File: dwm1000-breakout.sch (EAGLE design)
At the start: 9 parts, among them U2 DWM1000

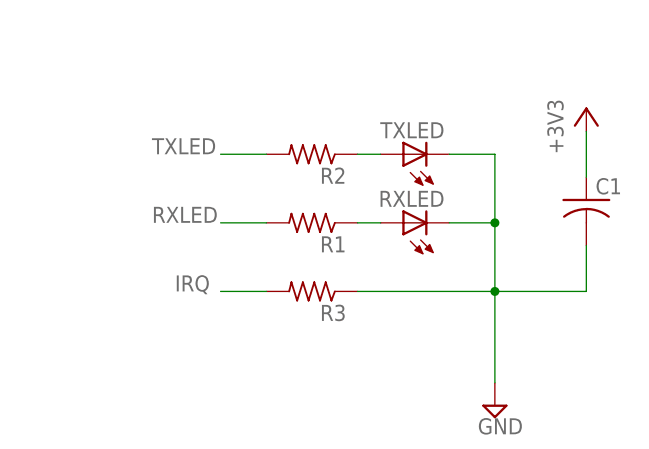
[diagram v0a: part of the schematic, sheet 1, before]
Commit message: renamed and laid out a little better i hope
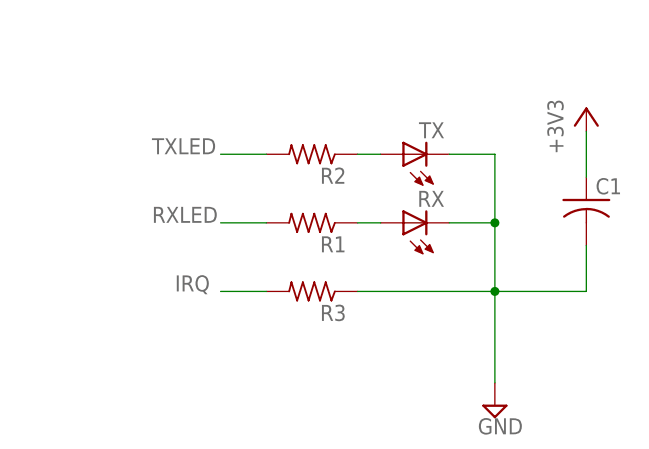
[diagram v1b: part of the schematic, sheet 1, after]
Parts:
- renumbered RXLED to RX, TXLED to TX
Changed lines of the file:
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@@
 <part name="R2" library="rcl" library_urn="urn:adsk.eagle:library:334" deviceset="R-US_" device="R1206"/>
 <part name="R3" library="rcl" library_urn="urn:adsk.eagle:library:334" deviceset="R-US_" device="R1206"/>
-<part name="RXLED" library="led" library_urn="urn:adsk.eagle:library:259" deviceset="LED" device="SMT1206"/>
-<part name="TXLED" library="led" library_urn="urn:adsk.eagle:library:259" deviceset="LED" device="SMT1206"/>
+<part name="RX" library="led" library_urn="urn:adsk.eagle:library:259" deviceset="LED" device="SMT1206"/>
+<part name="TX" library="led" library_urn="urn:adsk.eagle:library:259" deviceset="LED" device="SMT1206"/>
 <part name="SUPPLY1" library="supply2" library_urn="urn:adsk.eagle:library:372" deviceset="GND" device=""/>
 <part name="+3V1" library="supply1" library_urn="urn:adsk.eagle:library:371" deviceset="+3V3" device=""/>
@@
 <instance part="R2" gate="G$1" x="180.34" y="43.18" rot="R180"/>
 <instance part="R3" gate="G$1" x="180.34" y="27.94" rot="R180"/>
-<instance part="RXLED" gate="G$1" x="190.5" y="35.56" rot="R90"/>
-<instance part="TXLED" gate="G$1" x="190.5" y="43.18" rot="R90"/>
+<instance part="RX" gate="G$1" x="190.5" y="35.56" rot="R90"/>
+<instance part="TX" gate="G$1" x="190.5" y="43.18" rot="R90"/>
 <instance part="SUPPLY1" gate="GND" x="200.66" y="15.24"/>
 <instance part="+3V1" gate="G$1" x="210.82" y="48.26"/>
@@
 </segment>
 <segment>
-<pinref part="TXLED" gate="G$1" pin="C"/>
+<pinref part="TX" gate="G$1" pin="C"/>
 <wire x1="195.58" y1="43.18" x2="200.66" y2="43.18" width="0.1524" layer="91"/>
 <wire x1="200.66" y1="43.18" x2="200.66" y2="35.56" width="0.1524" layer="91"/>
 <pinref part="SUPPLY1" gate="GND" pin="GND"/>
-<pinref part="RXLED" gate="G$1" pin="C"/>
+<pinref part="RX" gate="G$1" pin="C"/>
 <wire x1="200.66" y1="35.56" x2="200.66" y2="27.94" width="0.1524" layer="91"/>
 <wire x1="200.66" y1="27.94" x2="200.66" y2="17.78" width="0.1524" layer="91"/>
@@
 <segment>
 <pinref part="R1" gate="G$1" pin="1"/>
-<pinref part="RXLED" gate="G$1" pin="A"/>
+<pinref part="RX" gate="G$1" pin="A"/>
 <wire x1="185.42" y1="35.56" x2="187.96" y2="35.56" width="0.1524" layer="91"/>
 </segment>
@@
 <segment>
 <pinref part="R2" gate="G$1" pin="1"/>
-<pinref part="TXLED" gate="G$1" pin="A"/>
+<pinref part="TX" gate="G$1" pin="A"/>
 <wire x1="185.42" y1="43.18" x2="187.96" y2="43.18" width="0.1524" layer="91"/>
 </segment>

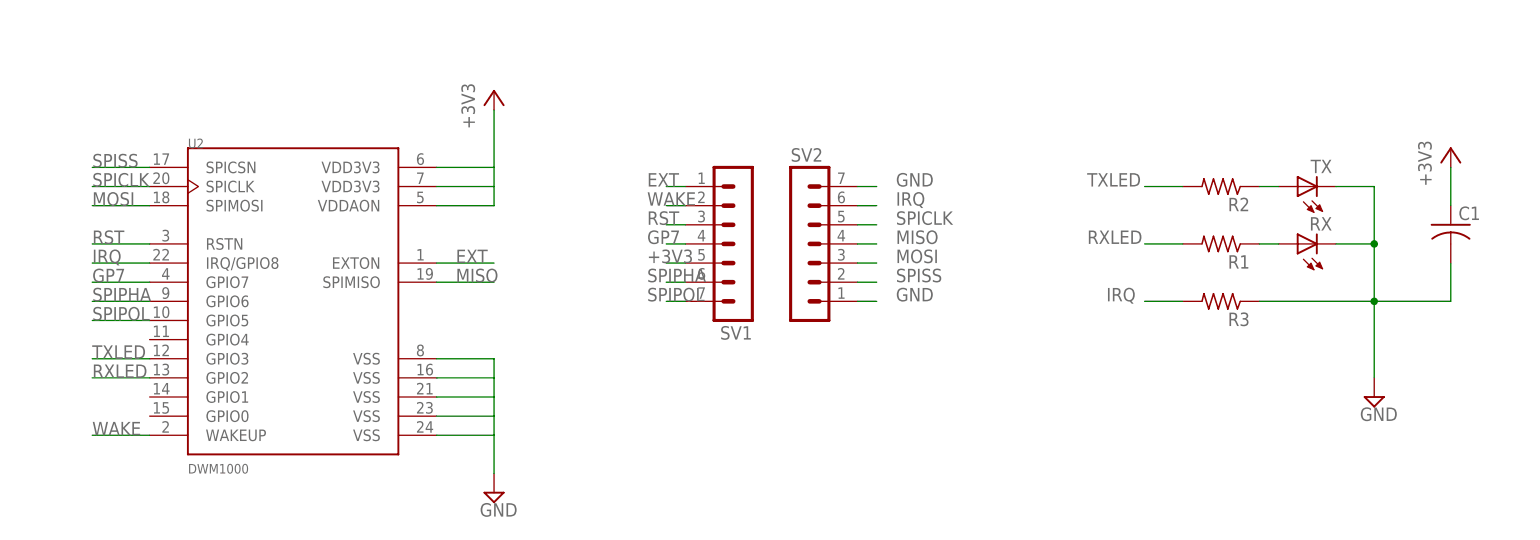
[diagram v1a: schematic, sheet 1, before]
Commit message: used oshpark's DRU file
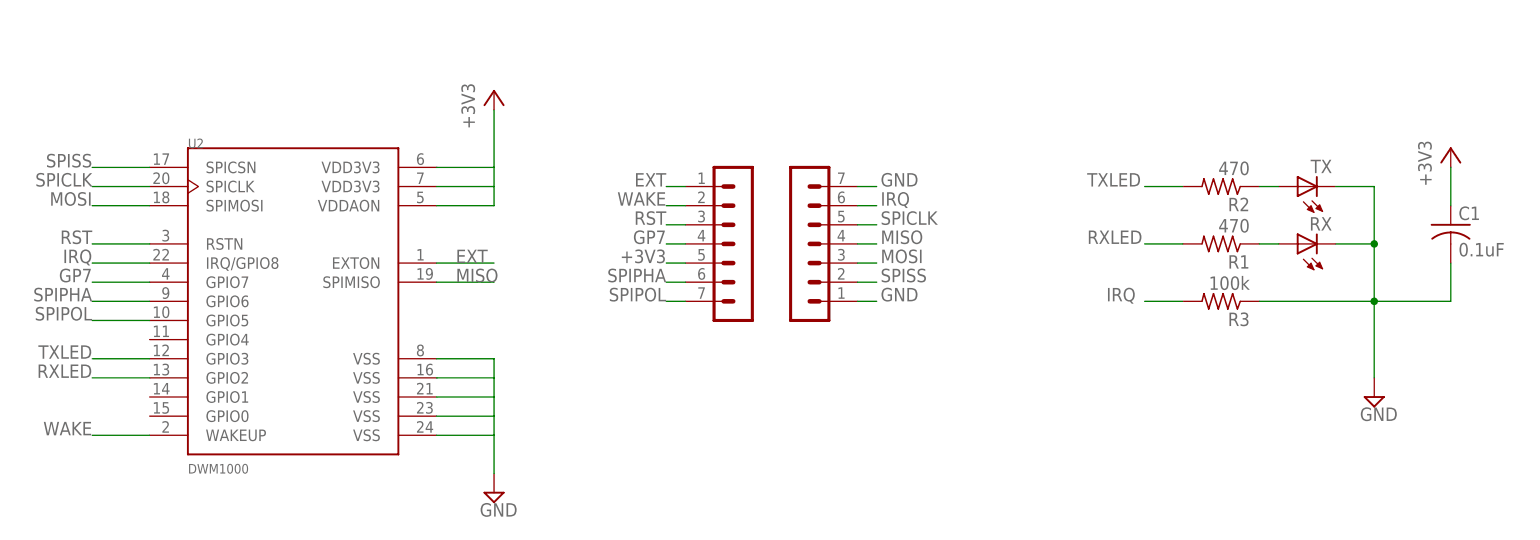
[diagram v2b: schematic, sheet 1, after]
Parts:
- C1: value (none) -> 0.1uF
- R1, R2: value (none) -> 470
- R3: value (none) -> 100k
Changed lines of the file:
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@@
 <setting verticaltext="up"/>
 </settings>
-<grid distance="0.1" unitdist="inch" unit="inch" style="dots" multiple="1" display="yes" altdistance="0.01" altunitdist="inch" altunit="inch"/>
+<grid distance="0.1" unitdist="inch" unit="inch" style="lines" multiple="1" display="no" altdistance="0.01" altunitdist="inch" altunit="inch"/>
 <layers>
 <layer number="1" name="Top" color="4" fill="1" visible="no" active="no"/>
@@
 <part name="SV1" library="con-lstb" library_urn="urn:adsk.eagle:library:162" deviceset="MA07-1" device=""/>
 <part name="SV2" library="con-lstb" library_urn="urn:adsk.eagle:library:162" deviceset="MA07-1" device=""/>
-<part name="C1" library="rcl" library_urn="urn:adsk.eagle:library:334" deviceset="C-US" device="C1206"/>
-<part name="R1" library="rcl" library_urn="urn:adsk.eagle:library:334" deviceset="R-US_" device="R1206"/>
-<part name="R2" library="rcl" library_urn="urn:adsk.eagle:library:334" deviceset="R-US_" device="R1206"/>
-<part name="R3" library="rcl" library_urn="urn:adsk.eagle:library:334" deviceset="R-US_" device="R1206"/>
+<part name="C1" library="rcl" library_urn="urn:adsk.eagle:library:334" deviceset="C-US" device="C1206" value="0.1uF"/>
+<part name="R1" library="rcl" library_urn="urn:adsk.eagle:library:334" deviceset="R-US_" device="R1206" value="470"/>
+<part name="R2" library="rcl" library_urn="urn:adsk.eagle:library:334" deviceset="R-US_" device="R1206" value="470"/>
+<part name="R3" library="rcl" library_urn="urn:adsk.eagle:library:334" deviceset="R-US_" device="R1206" value="100k"/>
 <part name="RX" library="led" library_urn="urn:adsk.eagle:library:259" deviceset="LED" device="SMT1206"/>
 <part name="TX" library="led" library_urn="urn:adsk.eagle:library:259" deviceset="LED" device="SMT1206"/>
@@
 </plain>
 <instances>
-<instance part="U2" gate="G$1" x="55.88" y="27.94"/>
+<instance part="U2" gate="G$1" x="55.88" y="27.94" smashed="yes">
+<attribute name="NAME" x="43.18" y="48.26" size="1.27" layer="95"/>
+<attribute name="VALUE" x="43.18" y="5.08" size="1.27" layer="96"/>
+</instance>
 <instance part="SUPPLY4" gate="GND" x="83.82" y="2.54"/>
 <instance part="+3V3" gate="G$1" x="83.82" y="55.88"/>
-<instance part="SV1" gate="1" x="116.84" y="35.56" rot="R180"/>
-<instance part="SV2" gate="1" x="124.46" y="35.56"/>
+<instance part="SV1" gate="1" x="116.84" y="35.56" smashed="yes" rot="R180">
+<attribute name="VALUE" x="118.11" y="48.26" size="1.778" layer="96" rot="R180"/>
+</instance>
+<instance part="SV2" gate="1" x="124.46" y="35.56" smashed="yes">
+<attribute name="VALUE" x="123.19" y="22.86" size="1.778" layer="96"/>
+</instance>
 <instance part="C1" gate="G$1" x="210.82" y="38.1"/>
 <instance part="R1" gate="G$1" x="180.34" y="35.56" rot="R180"/>
@@
 <pinref part="SV2" gate="1" pin="7"/>
 <wire x1="132.08" y1="43.18" x2="134.62" y2="43.18" width="0.1524" layer="91"/>
-<label x="137.16" y="43.18" size="1.778" layer="95"/>
+<label x="135.128" y="43.18" size="1.778" layer="95"/>
 </segment>
 <segment>
 <pinref part="SV2" gate="1" pin="1"/>
 <wire x1="132.08" y1="27.94" x2="134.62" y2="27.94" width="0.1524" layer="91"/>
-<label x="137.16" y="27.94" size="1.778" layer="95"/>
+<label x="135.128" y="27.94" size="1.778" layer="95"/>
 </segment>
 <segment>
@@
 <pinref part="SV1" gate="1" pin="5"/>
 <wire x1="109.22" y1="33.02" x2="106.68" y2="33.02" width="0.1524" layer="91"/>
-<label x="104.14" y="33.02" size="1.778" layer="95"/>
+<label x="106.68" y="33.02" size="1.778" layer="95" rot="MR0"/>
 </segment>
 <segment>
@@
 <pinref part="U2" gate="G$1" pin="SPIMOSI"/>
 <wire x1="38.1" y1="40.64" x2="30.48" y2="40.64" width="0.1524" layer="91"/>
-<label x="30.48" y="40.64" size="1.778" layer="95"/>
+<label x="30.48" y="40.64" size="1.778" layer="95" rot="MR0"/>
 </segment>
 <segment>
 <pinref part="SV2" gate="1" pin="3"/>
 <wire x1="132.08" y1="33.02" x2="134.62" y2="33.02" width="0.1524" layer="91"/>
-<label x="137.16" y="33.02" size="1.778" layer="95"/>
+<label x="135.128" y="33.02" size="1.778" layer="95"/>
 </segment>
 </net>
@@
 <pinref part="SV2" gate="1" pin="4"/>
 <wire x1="132.08" y1="35.56" x2="134.62" y2="35.56" width="0.1524" layer="91"/>
-<label x="137.16" y="35.56" size="1.778" layer="95"/>
+<label x="135.128" y="35.56" size="1.778" layer="95"/>
 </segment>
 </net>
@@
 <pinref part="U2" gate="G$1" pin="SPICLK"/>
 <wire x1="38.1" y1="43.18" x2="30.48" y2="43.18" width="0.1524" layer="91"/>
-<label x="30.48" y="43.18" size="1.778" layer="95"/>
+<label x="30.48" y="43.18" size="1.778" layer="95" rot="MR0"/>
 </segment>
 <segment>
 <pinref part="SV2" gate="1" pin="5"/>
 <wire x1="132.08" y1="38.1" x2="134.62" y2="38.1" width="0.1524" layer="91"/>
-<label x="137.16" y="38.1" size="1.778" layer="95"/>
+<label x="135.128" y="38.1" size="1.778" layer="95"/>
 </segment>
 </net>
@@
 <pinref part="U2" gate="G$1" pin="SPICSN"/>
 <wire x1="38.1" y1="45.72" x2="30.48" y2="45.72" width="0.1524" layer="91"/>
-<label x="30.48" y="45.72" size="1.778" layer="95"/>
+<label x="30.48" y="45.72" size="1.778" layer="95" rot="MR0"/>
 </segment>
 <segment>
 <pinref part="SV2" gate="1" pin="2"/>
 <wire x1="132.08" y1="30.48" x2="134.62" y2="30.48" width="0.1524" layer="91"/>
-<label x="137.16" y="30.48" size="1.778" layer="95"/>
+<label x="135.128" y="30.48" size="1.778" layer="95"/>
 </segment>
 </net>
@@
 <segment>
 <pinref part="U2" gate="G$1" pin="GPIO3"/>
-<label x="30.48" y="20.32" size="1.778" layer="95"/>
+<label x="30.48" y="20.32" size="1.778" layer="95" rot="MR0"/>
 <wire x1="38.1" y1="20.32" x2="30.48" y2="20.32" width="0.1524" layer="91"/>
 </segment>
@@
 <segment>
 <pinref part="U2" gate="G$1" pin="GPIO2"/>
-<label x="30.48" y="17.78" size="1.778" layer="95"/>
+<label x="30.48" y="17.78" size="1.778" layer="95" rot="MR0"/>
 <wire x1="38.1" y1="17.78" x2="30.48" y2="17.78" width="0.1524" layer="91"/>
 </segment>
@@
 <pinref part="SV1" gate="1" pin="1"/>
 <wire x1="109.22" y1="43.18" x2="106.68" y2="43.18" width="0.1524" layer="91"/>
-<label x="104.14" y="43.18" size="1.778" layer="95"/>
+<label x="106.68" y="43.18" size="1.778" layer="95" rot="MR0"/>
 </segment>
 <segment>
@@
 <pinref part="SV1" gate="1" pin="2"/>
 <wire x1="109.22" y1="40.64" x2="106.68" y2="40.64" width="0.1524" layer="91"/>
-<label x="104.14" y="40.64" size="1.778" layer="95"/>
+<label x="106.68" y="40.64" size="1.778" layer="95" rot="MR0"/>
 </segment>
 <segment>
 <pinref part="U2" gate="G$1" pin="WAKEUP"/>
 <wire x1="38.1" y1="10.16" x2="30.48" y2="10.16" width="0.1524" layer="91"/>
-<label x="30.48" y="10.16" size="1.778" layer="95"/>
+<label x="30.48" y="10.16" size="1.778" layer="95" rot="MR0"/>
 </segment>
 </net>
@@
 <pinref part="SV1" gate="1" pin="3"/>
 <wire x1="109.22" y1="38.1" x2="106.68" y2="38.1" width="0.1524" layer="91"/>
-<label x="104.14" y="38.1" size="1.778" layer="95"/>
+<label x="106.68" y="38.1" size="1.778" layer="95" rot="MR0"/>
 </segment>
 <segment>
 <pinref part="U2" gate="G$1" pin="RSTN"/>
 <wire x1="38.1" y1="35.56" x2="30.48" y2="35.56" width="0.1524" layer="91"/>
-<label x="30.48" y="35.56" size="1.778" layer="95"/>
+<label x="30.48" y="35.56" size="1.778" layer="95" rot="MR0"/>
 </segment>
 </net>
@@
 <pinref part="SV1" gate="1" pin="4"/>
 <wire x1="109.22" y1="35.56" x2="106.68" y2="35.56" width="0.1524" layer="91"/>
-<label x="104.14" y="35.56" size="1.778" layer="95"/>
+<label x="106.68" y="35.56" size="1.778" layer="95" rot="MR0"/>
 </segment>
 <segment>
 <pinref part="U2" gate="G$1" pin="GPIO7"/>
 <wire x1="38.1" y1="30.48" x2="30.48" y2="30.48" width="0.1524" layer="91"/>
-<label x="30.48" y="30.48" size="1.778" layer="95"/>
+<label x="30.48" y="30.48" size="1.778" layer="95" rot="MR0"/>
 </segment>
 </net>
@@
 <pinref part="SV1" gate="1" pin="6"/>
 <wire x1="109.22" y1="30.48" x2="106.68" y2="30.48" width="0.1524" layer="91"/>
-<label x="104.14" y="30.48" size="1.778" layer="95"/>
+<label x="106.68" y="30.48" size="1.778" layer="95" rot="MR0"/>
 </segment>
 <segment>
 <pinref part="U2" gate="G$1" pin="GPIO6"/>
 <wire x1="38.1" y1="27.94" x2="30.48" y2="27.94" width="0.1524" layer="91"/>
-<label x="30.48" y="27.94" size="1.778" layer="95"/>
+<label x="30.48" y="27.94" size="1.778" layer="95" rot="MR0"/>
 </segment>
 </net>
@@
 <pinref part="SV1" gate="1" pin="7"/>
 <wire x1="109.22" y1="27.94" x2="106.68" y2="27.94" width="0.1524" layer="91"/>
-<label x="104.14" y="27.94" size="1.778" layer="95"/>
+<label x="106.68" y="27.94" size="1.778" layer="95" rot="MR0"/>
 </segment>
 <segment>
 <pinref part="U2" gate="G$1" pin="GPIO5"/>
 <wire x1="38.1" y1="25.4" x2="30.48" y2="25.4" width="0.1524" layer="91"/>
-<label x="30.48" y="25.4" size="1.778" layer="95"/>
+<label x="30.48" y="25.4" size="1.778" layer="95" rot="MR0"/>
 </segment>
 </net>
@@
 <pinref part="SV2" gate="1" pin="6"/>
 <wire x1="132.08" y1="40.64" x2="134.62" y2="40.64" width="0.1524" layer="91"/>
-<label x="137.16" y="40.64" size="1.778" layer="95"/>
+<label x="135.128" y="40.64" size="1.778" layer="95"/>
 </segment>
 <segment>
@@
 <pinref part="U2" gate="G$1" pin="IRQ/GPIO8"/>
 <wire x1="38.1" y1="33.02" x2="30.48" y2="33.02" width="0.1524" layer="91"/>
-<label x="30.48" y="33.02" size="1.778" layer="95"/>
-</segment>
-</net>
+<label x="30.48" y="33.02" size="1.778" layer="95" rot="MR0"/>
+</segment>
+</net>

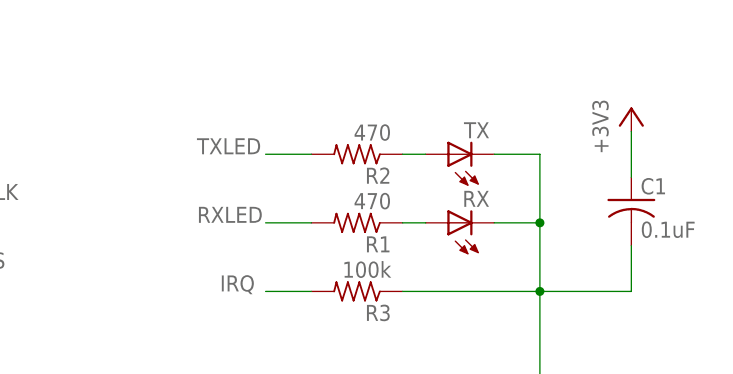
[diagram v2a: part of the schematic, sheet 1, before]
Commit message: added a power indicator LED
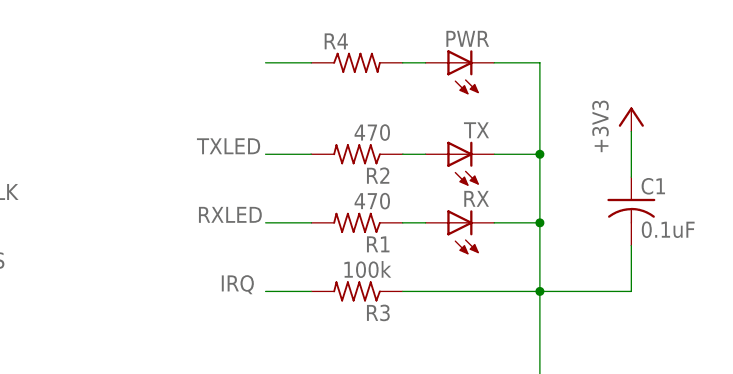
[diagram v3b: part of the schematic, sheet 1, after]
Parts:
- added PWR: (no value), led:LEDSMT1206
- added R4: (no value), rcl:R-US_R1206
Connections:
- new net N$3: PWR.A, R4.2
- net +3V3: now also R4.1
- net GND: now also PWR.C
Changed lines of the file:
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@@
 <part name="SUPPLY1" library="supply2" library_urn="urn:adsk.eagle:library:372" deviceset="GND" device=""/>
 <part name="+3V1" library="supply1" library_urn="urn:adsk.eagle:library:371" deviceset="+3V3" device=""/>
+<part name="PWR" library="led" library_urn="urn:adsk.eagle:library:259" deviceset="LED" device="SMT1206"/>
+<part name="R4" library="rcl" library_urn="urn:adsk.eagle:library:334" deviceset="R-US_" device="R1206"/>
 </parts>
 <sheets>
@@
 <instance part="SUPPLY1" gate="GND" x="200.66" y="15.24"/>
 <instance part="+3V1" gate="G$1" x="210.82" y="48.26"/>
+<instance part="PWR" gate="G$1" x="190.5" y="53.34" rot="R90"/>
+<instance part="R4" gate="G$1" x="180.34" y="53.34"/>
 </instances>
 <busses>
@@
 <wire x1="210.82" y1="33.02" x2="210.82" y2="27.94" width="0.1524" layer="91"/>
 <wire x1="210.82" y1="27.94" x2="200.66" y2="27.94" width="0.1524" layer="91"/>
+<pinref part="PWR" gate="G$1" pin="C"/>
+<wire x1="195.58" y1="53.34" x2="200.66" y2="53.34" width="0.1524" layer="91"/>
+<wire x1="200.66" y1="53.34" x2="200.66" y2="43.18" width="0.1524" layer="91"/>
+<junction x="200.66" y="43.18"/>
 </segment>
 </net>
@@
 <pinref part="+3V1" gate="G$1" pin="+3V3"/>
 </segment>
+<segment>
+<pinref part="R4" gate="G$1" pin="1"/>
+<wire x1="175.26" y1="53.34" x2="170.18" y2="53.34" width="0.1524" layer="91"/>
+</segment>
 </net>
 <net name="MOSI" class="0">
@@
 </segment>
 </net>
+<net name="N$3" class="0">
+<segment>
+<pinref part="R4" gate="G$1" pin="2"/>
+<pinref part="PWR" gate="G$1" pin="A"/>
+<wire x1="185.42" y1="53.34" x2="187.96" y2="53.34" width="0.1524" layer="91"/>
+</segment>
+</net>
